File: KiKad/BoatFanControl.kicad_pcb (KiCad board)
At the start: 2 copper layers, 34 x 34.8 mm, 13 parts, among them J1 Batt, J2 Reset, Q1 IRLZ14, SW1 SW_Push, U1 Digispark

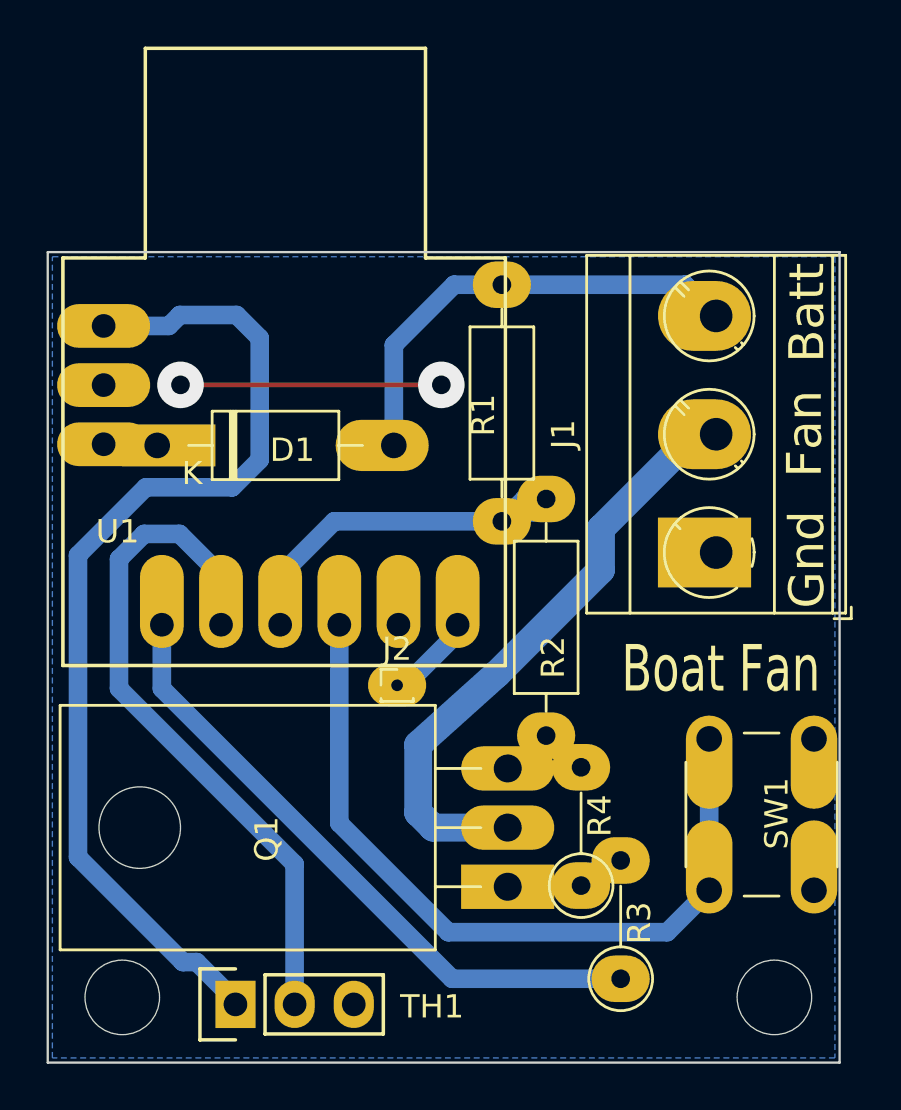
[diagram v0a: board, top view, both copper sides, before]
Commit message: PCB work, add flyback diode
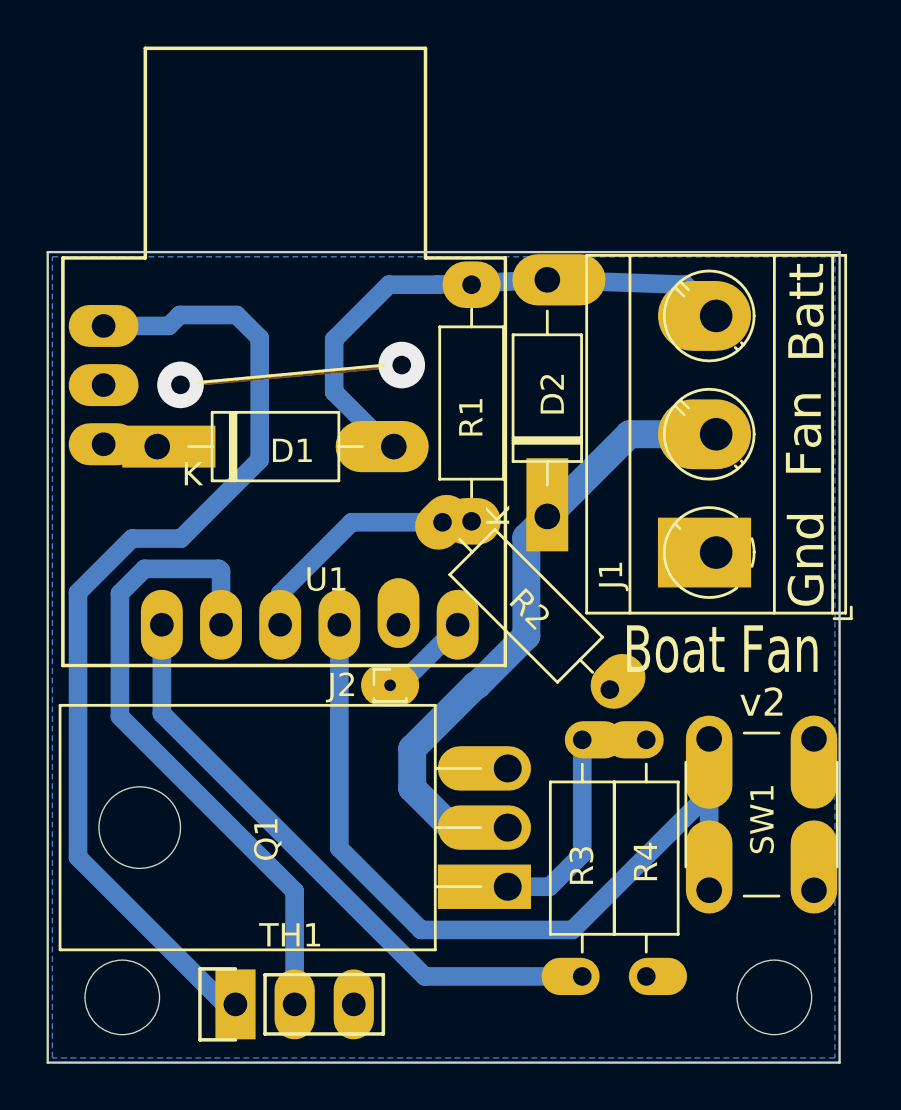
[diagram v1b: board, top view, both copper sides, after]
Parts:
- added D2: 1N4007, Diode_THT:D_DO-41_SOD81_P10.16mm_Horizontal, F.Cu at (106.5, 76.3)
- R3, R4: footprint Resistor_THT:R_Axial_DIN0207_L6.3mm_D2.5mm_P5.08mm_Vertical -> Resistor_THT:R_Axial_DIN0207_L6.3mm_D2.5mm_P10.16mm_Horizontal
- TH1: footprint sensors:DHT11_Temperature_Humidity -> sensorz:DHT11_Temperature_Humidity
- U1: footprint digi:Digispark -> mcuz:Digispark
- moved R4 6.86 mm to (110.7, 85.9), turned to 270 degrees
- moved R2 4.56 mm to (102.0, 76.6), turned to 315 degrees
- moved R3 1.65 mm to (108.0, 96.1)
- moved R1 1.30 mm to (103.2, 66.4)
- moved J2 0.30 mm to (99.7, 83.6)
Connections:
- net FAN-gnd renamed FAN-GND
- net LED renamed fan-pwm
- net Vin-sense renamed Vsense
- D1 pad 1: +BATT -> Vin
- D1 pad 2: Vin -> Vbatt
- J1 pad 3: Vin -> Vbatt
- R1 pad 1: Vin -> Vbatt
- U1 pad 7: +BATT -> Vin
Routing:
- net Vbatt: track 0.00 -> 23.7 mm
- net Vin: track 19.8 -> 2.34 mm
- net Net-(Q1-Pad1): track 5.32 -> 11.4 mm
- net Vsense: track 15.7 -> 10.8 mm
- net button: track 33.6 -> 38.2 mm
- net GND: track 13.9 -> 9.54 mm
- net +BATT: track 2.32 -> 0.00 mm
- net DHT11: track 29.9 -> 27.9 mm
- net FAN-GND: track 26.3 -> 27.6 mm
- net fan-pwm: track 27.6 -> 26.5 mm
- net +5V: track 44.5 -> 43.5 mm
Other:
- board text added: "v2"

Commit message: Refresh the PCB
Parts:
- moved D2 10.0 mm to (106.7, 66.3), turned to 270 degrees
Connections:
- D2 pad 1: FAN-GND -> Vbatt
- D2 pad 2: Vbatt -> FAN-GND
